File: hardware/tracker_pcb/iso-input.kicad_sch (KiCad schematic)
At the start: 5 parts, among them Q1 LTV-817S-TA1

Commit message: Work
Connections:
- net IN- is gone; now on net GND: D5.2 (A), Q1.2
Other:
- moved on the sheet: D5
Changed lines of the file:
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@@
 	)
 	(junction
-		(at 120.65 90.17)
+		(at 127 85.09)
 		(diameter 0)
 		(color 0 0 0 0)
 	)
 	(junction
-		(at 120.65 85.09)
+		(at 146.05 97.79)
 		(diameter 0)
 		(color 0 0 0 0)
 	)
-	(wire
-		(pts
-			(xy 95.25 87.63) (xy 90.17 87.63)
-		)
-		(stroke
-			(width 0)
-			(type default)
-		)
+	(junction
+		(at 127 97.79)
+		(diameter 0)
+		(color 0 0 0 0)
 	)
 	(wire
@@
 	(wire
 		(pts
+			(xy 146.05 97.79) (xy 146.05 90.17)
+		)
+		(stroke
+			(width 0)
+			(type default)
+		)
+	)
+	(wire
+		(pts
 			(xy 102.87 85.09) (xy 90.17 85.09)
 		)
@@
 	(wire
 		(pts
-			(xy 130.81 85.09) (xy 120.65 85.09)
-		)
-		(stroke
-			(width 0)
-			(type default)
-		)
-	)
-	(wire
-		(pts
-			(xy 95.25 90.17) (xy 95.25 87.63)
+			(xy 130.81 85.09) (xy 127 85.09)
+		)
+		(stroke
+			(width 0)
+			(type default)
+		)
+	)
+	(wire
+		(pts
+			(xy 173.99 90.17) (xy 173.99 97.79)
+		)
+		(stroke
+			(width 0)
+			(type default)
+		)
+	)
+	(wire
+		(pts
+			(xy 127 97.79) (xy 127 102.87)
 		)
 		(stroke
@@
 	(wire
 		(pts
+			(xy 127 88.9) (xy 127 85.09)
+		)
+		(stroke
+			(width 0)
+			(type default)
+		)
+	)
+	(wire
+		(pts
 			(xy 179.07 68.58) (xy 179.07 71.12)
 		)
@@
 	(wire
 		(pts
-			(xy 95.25 90.17) (xy 120.65 90.17)
-		)
-		(stroke
-			(width 0)
-			(type default)
-		)
-	)
-	(wire
-		(pts
 			(xy 179.07 85.09) (xy 187.96 85.09)
 		)
@@
 	(wire
 		(pts
-			(xy 110.49 85.09) (xy 120.65 85.09)
-		)
-		(stroke
-			(width 0)
-			(type default)
-		)
-	)
-	(wire
-		(pts
-			(xy 146.05 90.17) (xy 120.65 90.17)
-		)
-		(stroke
-			(width 0)
-			(type default)
-		)
-	)
-	(wire
-		(pts
-			(xy 179.07 97.79) (xy 179.07 90.17)
-		)
-		(stroke
-			(width 0)
-			(type default)
-		)
-	)
-	(wire
-		(pts
-			(xy 179.07 90.17) (xy 173.99 90.17)
+			(xy 110.49 85.09) (xy 127 85.09)
+		)
+		(stroke
+			(width 0)
+			(type default)
+		)
+	)
+	(wire
+		(pts
+			(xy 146.05 97.79) (xy 127 97.79)
+		)
+		(stroke
+			(width 0)
+			(type default)
+		)
+	)
+	(wire
+		(pts
+			(xy 173.99 97.79) (xy 146.05 97.79)
+		)
+		(stroke
+			(width 0)
+			(type default)
+		)
+	)
+	(wire
+		(pts
+			(xy 127 97.79) (xy 127 93.98)
 		)
 		(stroke
@@
 			)
 			(justify left)
-		)
-	)
-	(hierarchical_label "IN-"
-		(shape passive)
-		(at 90.17 87.63 180)
-		(effects
-			(font
-				(size 1.27 1.27)
-			)
-			(justify right)
 		)
 	)
@@
 	)
 	(symbol
-		(lib_id "ESP32-C6-EVB_Rev_A:GND")
-		(at 179.07 97.79 0)
-		(unit 1)
-		(exclude_from_sim no)
-		(in_bom yes)
-		(on_board yes)
-		(dnp no)
-		(property "Reference" "#PWR010"
-			(at 179.07 104.14 0)
-			(effects
-				(font
-					(size 1.27 1.27)
-				)
-				(hide yes)
-			)
-		)
-		(property "Value" "GND"
-			(at 179.07 102.87 90)
-			(effects
-				(font
-					(size 1.27 1.27)
-				)
-			)
-		)
-		(property "Footprint" ""
-			(at 179.07 97.79 0)
-			(effects
-				(font
-					(size 1.524 1.524)
-				)
-			)
-		)
-		(property "Datasheet" ""
-			(at 179.07 97.79 0)
-			(effects
-				(font
-					(size 1.524 1.524)
-				)
-			)
-		)
-		(property "Description" ""
-			(at 179.07 97.79 0)
-			(effects
-				(font
-					(size 1.27 1.27)
-				)
-			)
-		)
-		(pin "1"
-		)
-		(instances
-			(project "tracker_pcb"
-				(path "/6aaa9514-f94e-4843-90d0-16960e4e49cb/45c78875-26ba-4b22-bc82-79a51b704824"
-					(reference "#PWR010")
-					(unit 1)
-				)
-			)
-		)
-	)
-	(symbol
 		(lib_id "Device:R_US")
 		(at 179.07 74.93 0)
@@
 	(symbol
 		(lib_id "ESP32-C6-EVB_Rev_A:D_Small")
-		(at 120.65 87.63 90)
+		(at 127 91.44 90)
 		(mirror x)
 		(unit 1)
@@
 		(dnp no)
 		(property "Reference" "D5"
-			(at 119.38 82.55 90)
+			(at 125.73 86.36 90)
 			(effects
 				(font
@@
 		)
 		(property "Value" "1N4148W(SOD-123)"
-			(at 110.49 92.71 90)
+			(at 105.664 93.98 90)
 			(effects
 				(font
@@
 		)
 		(property "Footprint" "Diode_SMD:D_0603_1608Metric"
-			(at 118.4148 89.9414 90)
+			(at 124.7648 93.7514 90)
 			(effects
 				(font
@@
 		)
 		(property "Datasheet" ""
-			(at 120.65 87.63 90)
+			(at 127 91.44 90)
 			(effects
 				(font
@@
 		)
 		(property "Description" ""
-			(at 120.65 87.63 0)
+			(at 127 91.44 0)
 			(effects
 				(font
@@
 					(unit 1)
 				)
+			)
+		)
+	)
+	(symbol
+		(lib_name "GND_1")
+		(lib_id "ESP32-C6-EVB_Rev_A:GND")
+		(at 127 102.87 0)
+		(unit 1)
+		(exclude_from_sim no)
+		(in_bom yes)
+		(on_board yes)
+		(dnp no)
+		(property "Reference" "#PWR09"
+			(at 127 109.22 0)
+			(effects
+				(font
+					(size 1.27 1.27)
+				)
+				(hide yes)
+			)
+		)
+		(property "Value" "GND"
+			(at 127 107.95 90)
+			(effects
+				(font
+					(size 1.27 1.27)
+				)
+				(hide yes)
+			)
+		)
+		(property "Footprint" ""
+			(at 127 102.87 0)
+			(effects
+				(font
+					(size 1.524 1.524)
+				)
+				(hide yes)
+			)
+		)
+		(property "Datasheet" ""
+			(at 127 102.87 0)
+			(effects
+				(font
+					(size 1.524 1.524)
+				)
+				(hide yes)
+			)
+		)
+		(property "Description" ""
+			(at 127 102.87 0)
+			(effects
+				(font
+					(size 1.27 1.27)
+				)
+				(hide yes)
+			)
+		)
+		(pin "1"
+		)
+		(instances
+			(project "tracker_pcb"
+				(path "/6aaa9514-f94e-4843-90d0-16960e4e49cb/45c78875-26ba-4b22-bc82-79a51b704824"
+					(reference "#PWR09")
+					(unit 1)
+				)

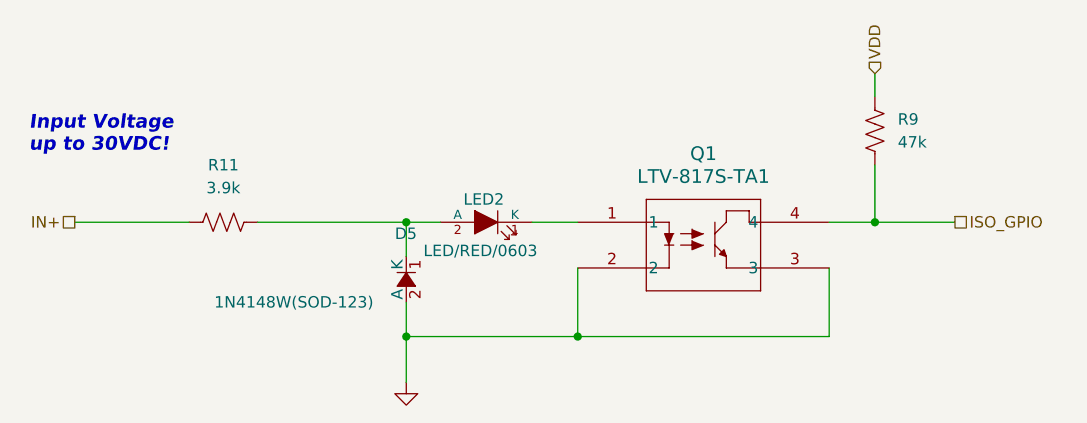
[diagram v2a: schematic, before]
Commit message: Complete but optos are using 5v pullups instead of 3v3.  No bueno
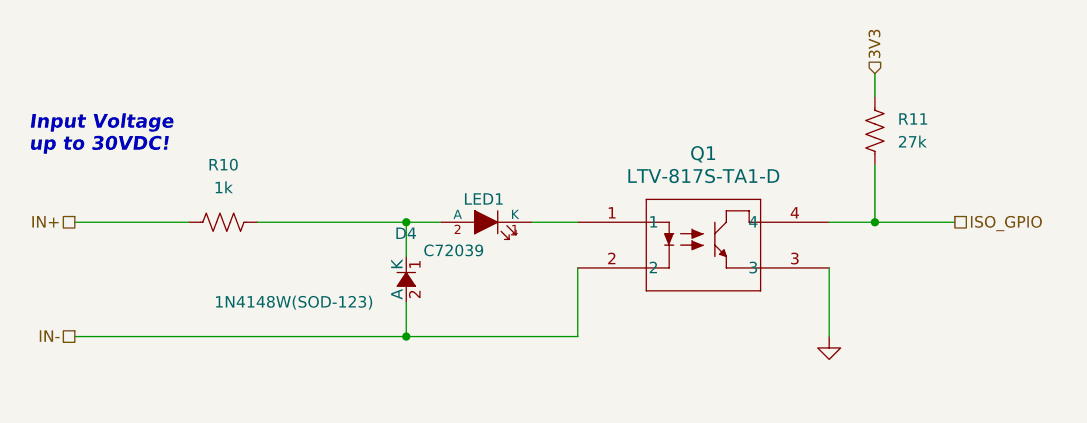
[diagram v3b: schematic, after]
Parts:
- D4: renamed from D5; footprint Diode_SMD:D_0603_1608Metric -> Diode_SMD:D_SOD-123
- LED1: renamed from LED2; value LED/RED/0603 -> C72039
- Q1: value LTV-817S-TA1 -> LTV-817S-TA1-D
- R10: renamed from R11; value 3.9k -> 1k
- R11: renamed from R9; value 47k -> 27k
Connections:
- net GND: no longer D4.2 (A), Q1.2
- net VDD renamed 3V3
- new net IN-: D4.2 (A), Q1.2
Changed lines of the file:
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@@
-	)
-	(junction
-		(at 146.05 97.79)
-		(diameter 0)
-		(color 0 0 0 0)
 	)
 	(junction
@@
 	(wire
 		(pts
-			(xy 127 97.79) (xy 127 102.87)
+			(xy 90.17 97.79) (xy 127 97.79)
 		)
 		(stroke
@@
 	(wire
 		(pts
-			(xy 146.05 97.79) (xy 127 97.79)
-		)
-		(stroke
-			(width 0)
-			(type default)
-		)
-	)
-	(wire
-		(pts
-			(xy 173.99 97.79) (xy 146.05 97.79)
-		)
-		(stroke
-			(width 0)
-			(type default)
-		)
-	)
-	(wire
-		(pts
-			(xy 127 97.79) (xy 127 93.98)
+			(xy 127 97.79) (xy 146.05 97.79)
+		)
+		(stroke
+			(width 0)
+			(type default)
+		)
+	)
+	(wire
+		(pts
+			(xy 127 93.98) (xy 127 97.79)
 		)
 		(stroke
@@
 		)
 	)
-	(hierarchical_label "VDD"
+	(hierarchical_label "IN-"
+		(shape passive)
+		(at 90.17 97.79 180)
+		(effects
+			(font
+				(size 1.27 1.27)
+			)
+			(justify right)
+		)
+	)
+	(hierarchical_label "3V3"
 		(shape input)
 		(at 179.07 68.58 90)
@@
 		(on_board yes)
 		(dnp no)
-		(property "Reference" "LED2"
+		(property "Reference" "LED1"
 			(at 133.35 82.55 0)
 			(effects
@@
 			)
 		)
-		(property "Value" "LED/RED/0603"
+		(property "Value" "C72039"
 			(at 128.905 88.265 0)
 			(effects
@@
 		(instances
 			(project "tracker_pcb"
-				(path "/6aaa9514-f94e-4843-90d0-16960e4e49cb/00dc7bbc-6624-4dc0-8ef8-528baecc0d57"
+				(path "/6aaa9514-f94e-4843-90d0-16960e4e49cb/04328898-976a-48a2-86bf-9938cb4aefd5"
+					(reference "LED2")
+					(unit 1)
+				)
+				(path "/6aaa9514-f94e-4843-90d0-16960e4e49cb/45a2292e-2f51-4a4c-a627-74180fb6fdfe"
+					(reference "LED4")
+					(unit 1)
+				)
+				(path "/6aaa9514-f94e-4843-90d0-16960e4e49cb/45c78875-26ba-4b22-bc82-79a51b704824"
+					(reference "LED1")
+					(unit 1)
+				)
+				(path "/6aaa9514-f94e-4843-90d0-16960e4e49cb/b128d80c-4aa3-4c05-bd4f-543db8edd72e"
 					(reference "LED3")
-					(unit 1)
-				)
-				(path "/6aaa9514-f94e-4843-90d0-16960e4e49cb/04328898-976a-48a2-86bf-9938cb4aefd5"
-					(reference "LED1")
-					(unit 1)
-				)
-				(path "/6aaa9514-f94e-4843-90d0-16960e4e49cb/45c78875-26ba-4b22-bc82-79a51b704824"
-					(reference "LED2")
 					(unit 1)
 				)
@@
 		(dnp no)
 		(fields_autoplaced yes)
-		(property "Reference" "R11"
+		(property "Reference" "R10"
 			(at 106.68 78.74 90)
 			(effects
@@
 			)
 		)
-		(property "Value" "3.9k"
+		(property "Value" "1k"
 			(at 106.68 81.28 90)
 			(effects
@@
 		(instances
 			(project "tracker_pcb"
-				(path "/6aaa9514-f94e-4843-90d0-16960e4e49cb/00dc7bbc-6624-4dc0-8ef8-528baecc0d57"
-					(reference "R14")
-					(unit 1)
-				)
 				(path "/6aaa9514-f94e-4843-90d0-16960e4e49cb/04328898-976a-48a2-86bf-9938cb4aefd5"
 					(reference "R12")
 					(unit 1)
 				)
+				(path "/6aaa9514-f94e-4843-90d0-16960e4e49cb/45a2292e-2f51-4a4c-a627-74180fb6fdfe"
+					(reference "R16")
+					(unit 1)
+				)
 				(path "/6aaa9514-f94e-4843-90d0-16960e4e49cb/45c78875-26ba-4b22-bc82-79a51b704824"
-					(reference "R11")
+					(reference "R10")
+					(unit 1)
+				)
+				(path "/6aaa9514-f94e-4843-90d0-16960e4e49cb/b128d80c-4aa3-4c05-bd4f-543db8edd72e"
+					(reference "R14")
+					(unit 1)
+				)
+			)
+		)
+	)
+	(symbol
+		(lib_name "GND_1")
+		(lib_id "ESP32-C6-EVB_Rev_A:GND")
+		(at 173.99 97.79 0)
+		(unit 1)
+		(exclude_from_sim no)
+		(in_bom yes)
+		(on_board yes)
+		(dnp no)
+		(property "Reference" "#PWR015"
+			(at 173.99 104.14 0)
+			(effects
+				(font
+					(size 1.27 1.27)
+				)
+				(hide yes)
+			)
+		)
+		(property "Value" "GND"
+			(at 173.99 102.87 90)
+			(effects
+				(font
+					(size 1.27 1.27)
+				)
+				(hide yes)
+			)
+		)
+		(property "Footprint" ""
+			(at 173.99 97.79 0)
+			(effects
+				(font
+					(size 1.524 1.524)
+				)
+				(hide yes)
+			)
+		)
+		(property "Datasheet" ""
+			(at 173.99 97.79 0)
+			(effects
+				(font
+					(size 1.524 1.524)
+				)
+				(hide yes)
+			)
+		)
+		(property "Description" ""
+			(at 173.99 97.79 0)
+			(effects
+				(font
+					(size 1.27 1.27)
+				)
+				(hide yes)
+			)
+		)
+		(pin "1"
+		)
+		(instances
+			(project "tracker_pcb"
+				(path "/6aaa9514-f94e-4843-90d0-16960e4e49cb/04328898-976a-48a2-86bf-9938cb4aefd5"
+					(reference "#PWR016")
+					(unit 1)
+				)
+				(path "/6aaa9514-f94e-4843-90d0-16960e4e49cb/45a2292e-2f51-4a4c-a627-74180fb6fdfe"
+					(reference "#PWR018")
+					(unit 1)
+				)
+				(path "/6aaa9514-f94e-4843-90d0-16960e4e49cb/45c78875-26ba-4b22-bc82-79a51b704824"
+					(reference "#PWR015")
+					(unit 1)
+				)
+				(path "/6aaa9514-f94e-4843-90d0-16960e4e49cb/b128d80c-4aa3-4c05-bd4f-543db8edd72e"
+					(reference "#PWR017")
 					(unit 1)
 				)
@@
 		(dnp no)
 		(fields_autoplaced yes)
-		(property "Reference" "R9"
+		(property "Reference" "R11"
 			(at 181.61 73.6599 0)
 			(effects
@@
 			)
 		)
-		(property "Value" "47k"
+		(property "Value" "27k"
 			(at 181.61 76.1999 0)
 			(effects
@@
 		(instances
 			(project "tracker_pcb"
-				(path "/6aaa9514-f94e-4843-90d0-16960e4e49cb/00dc7bbc-6624-4dc0-8ef8-528baecc0d57"
-					(reference "R15")
-					(unit 1)
-				)
 				(path "/6aaa9514-f94e-4843-90d0-16960e4e49cb/04328898-976a-48a2-86bf-9938cb4aefd5"
 					(reference "R13")
 					(unit 1)
 				)
+				(path "/6aaa9514-f94e-4843-90d0-16960e4e49cb/45a2292e-2f51-4a4c-a627-74180fb6fdfe"
+					(reference "R17")
+					(unit 1)
+				)
 				(path "/6aaa9514-f94e-4843-90d0-16960e4e49cb/45c78875-26ba-4b22-bc82-79a51b704824"
-					(reference "R9")
+					(reference "R11")
+					(unit 1)
+				)
+				(path "/6aaa9514-f94e-4843-90d0-16960e4e49cb/b128d80c-4aa3-4c05-bd4f-543db8edd72e"
+					(reference "R15")
 					(unit 1)
 				)
@@
 			)
 		)
-		(property "Value" "LTV-817S-TA1"
+		(property "Value" "LTV-817S-TA1-D"
 			(at 160.02 80.01 0)
 			(effects
@@
 			)
 		)
-		(property "Datasheet" "LTV-817S-TA1"
+		(property "Datasheet" "https://optoelectronics.liteon.com/upload/download/DS-70-96-0016/LTV-8X7%20series%20201610%20.pdf"
 			(at 146.05 85.09 0)
 			(effects
@@
 		(instances
 			(project "tracker_pcb"
-				(path "/6aaa9514-f94e-4843-90d0-16960e4e49cb/00dc7bbc-6624-4dc0-8ef8-528baecc0d57"
-					(reference "Q3")
-					(unit 1)
-				)
 				(path "/6aaa9514-f94e-4843-90d0-16960e4e49cb/04328898-976a-48a2-86bf-9938cb4aefd5"
 					(reference "Q2")
 					(unit 1)
 				)
+				(path "/6aaa9514-f94e-4843-90d0-16960e4e49cb/45a2292e-2f51-4a4c-a627-74180fb6fdfe"
+					(reference "Q4")
+					(unit 1)
+				)
 				(path "/6aaa9514-f94e-4843-90d0-16960e4e49cb/45c78875-26ba-4b22-bc82-79a51b704824"
 					(reference "Q1")
+					(unit 1)
+				)
+				(path "/6aaa9514-f94e-4843-90d0-16960e4e49cb/b128d80c-4aa3-4c05-bd4f-543db8edd72e"
+					(reference "Q3")
 					(unit 1)
 				)
@@
 		(on_board yes)
 		(dnp no)
-		(property "Reference" "D5"
+		(property "Reference" "D4"
 			(at 125.73 86.36 90)
 			(effects
@@
 			)
 		)
-		(property "Footprint" "Diode_SMD:D_0603_1608Metric"
+		(property "Footprint" "Diode_SMD:D_SOD-123"
 			(at 124.7648 93.7514 90)
 			(effects
@@
 		(instances
 			(project "tracker_pcb"
-				(path "/6aaa9514-f94e-4843-90d0-16960e4e49cb/00dc7bbc-6624-4dc0-8ef8-528baecc0d57"
+				(path "/6aaa9514-f94e-4843-90d0-16960e4e49cb/04328898-976a-48a2-86bf-9938cb4aefd5"
+					(reference "D5")
+					(unit 1)
+				)
+				(path "/6aaa9514-f94e-4843-90d0-16960e4e49cb/45a2292e-2f51-4a4c-a627-74180fb6fdfe"
+					(reference "D7")
+					(unit 1)
+				)
+				(path "/6aaa9514-f94e-4843-90d0-16960e4e49cb/45c78875-26ba-4b22-bc82-79a51b704824"
+					(reference "D4")
+					(unit 1)
+				)
+				(path "/6aaa9514-f94e-4843-90d0-16960e4e49cb/b128d80c-4aa3-4c05-bd4f-543db8edd72e"
 					(reference "D6")
 					(unit 1)
 				)
-				(path "/6aaa9514-f94e-4843-90d0-16960e4e49cb/04328898-976a-48a2-86bf-9938cb4aefd5"
-					(reference "D4")
-					(unit 1)
-				)
-				(path "/6aaa9514-f94e-4843-90d0-16960e4e49cb/45c78875-26ba-4b22-bc82-79a51b704824"
-					(reference "D5")
-					(unit 1)
-				)
-			)
-		)
-	)
-	(symbol
-		(lib_name "GND_1")
-		(lib_id "ESP32-C6-EVB_Rev_A:GND")
-		(at 127 102.87 0)
-		(unit 1)
-		(exclude_from_sim no)
-		(in_bom yes)
-		(on_board yes)
-		(dnp no)
-		(property "Reference" "#PWR09"
-			(at 127 109.22 0)
-			(effects
-				(font
-					(size 1.27 1.27)
-				)
-				(hide yes)
-			)
-		)
-		(property "Value" "GND"
-			(at 127 107.95 90)
-			(effects
-				(font
-					(size 1.27 1.27)
-				)
-				(hide yes)
-			)
-		)
-		(property "Footprint" ""
-			(at 127 102.87 0)
-			(effects
-				(font
-					(size 1.524 1.524)
-				)
-				(hide yes)
-			)
-		)
-		(property "Datasheet" ""
-			(at 127 102.87 0)
-			(effects
-				(font
-					(size 1.524 1.524)
-				)
-				(hide yes)
-			)
-		)
-		(property "Description" ""
-			(at 127 102.87 0)
-			(effects
-				(font
-					(size 1.27 1.27)
-				)
-				(hide yes)
-			)
-		)
-		(pin "1"
-		)
-		(instances
-			(project "tracker_pcb"
-				(path "/6aaa9514-f94e-4843-90d0-16960e4e49cb/00dc7bbc-6624-4dc0-8ef8-528baecc0d57"
-					(reference "#PWR013")
-					(unit 1)
-				)
-				(path "/6aaa9514-f94e-4843-90d0-16960e4e49cb/04328898-976a-48a2-86bf-9938cb4aefd5"
-					(reference "#PWR011")
-					(unit 1)
-				)
-				(path "/6aaa9514-f94e-4843-90d0-16960e4e49cb/45c78875-26ba-4b22-bc82-79a51b704824"
-					(reference "#PWR09")
-					(unit 1)
-				)

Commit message: WIP
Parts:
- R10: footprint Resistor_SMD:R_0603_1608Metric -> Resistor_SMD:R_0805_2012Metric_Pad1.20x1.40mm_HandSolder
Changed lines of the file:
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@@
 			)
 		)
-		(property "Footprint" "Resistor_SMD:R_0603_1608Metric"
+		(property "Footprint" "Resistor_SMD:R_0805_2012Metric_Pad1.20x1.40mm_HandSolder"
 			(at 106.934 84.074 90)
 			(effects
